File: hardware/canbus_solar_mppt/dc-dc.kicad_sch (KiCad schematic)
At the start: 22 parts

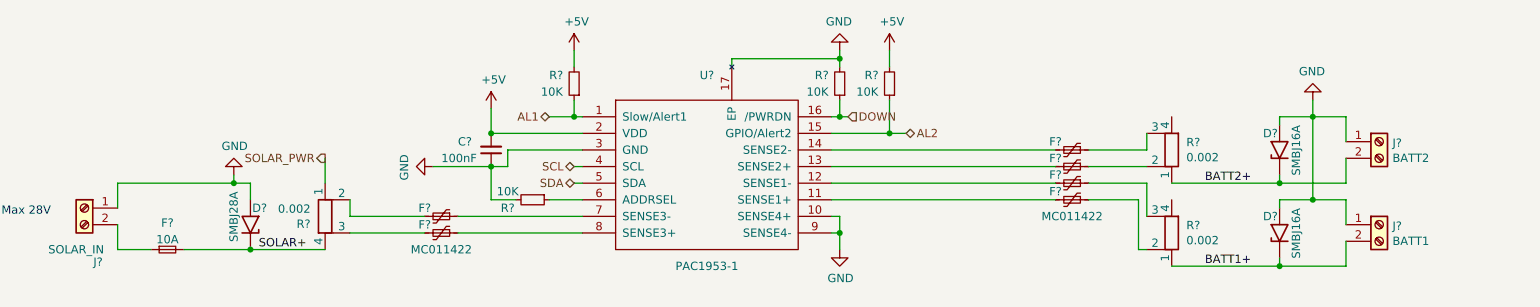
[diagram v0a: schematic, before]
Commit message: Add feedthrough capacitors as EMI filters on power inputs
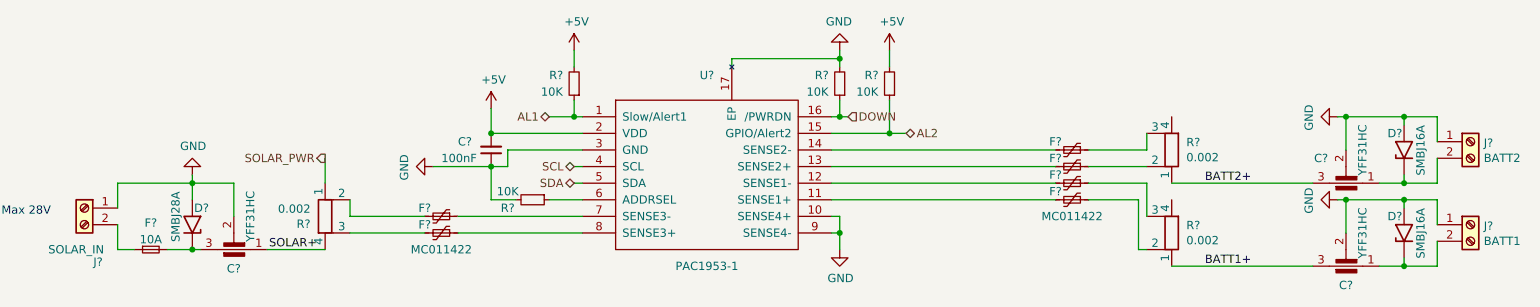
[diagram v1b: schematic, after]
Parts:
- added C? (x3): YFF31HC, local:C_filter_1206, symbol Device:C_Feedthrough
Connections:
- net BATT1+: now also C?.3; no longer D?.1 (A1), J?.2 (Pin_2)
- net BATT2+: now also C?.3; no longer D?.1 (A1), J?.2 (Pin_2)
- net GND: now also C?.2, C?.2, C?.2
- net SOLAR+: now also C?.1; no longer D?.1 (A1), F?.2
- new net: C?.1, D?.1 (A1), J?.2 (Pin_2) (x2)
- new net: C?.3, D?.1 (A1), F?.2
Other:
- moved on the sheet: D?, F?, J?

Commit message: WIP: complete DC/DC engine
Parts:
- added C?: 10µ25V, Capacitor_SMD:C_1206_3216Metric_Pad1.33x1.80mm_HandSolder, symbol Device:C_Small
- added C? (x4): 330µ35V, Capacitor_SMD:CP_Elec_10x12.6, symbol Device:C_Polarized_Small
- added C? (x2): 100nF, Capacitor_SMD:C_0805_2012Metric_Pad1.18x1.45mm_HandSolder, symbol Device:C_Small
- added C? (x2): 4.7µ50V, Capacitor_SMD:C_1206_3216Metric_Pad1.33x1.80mm_HandSolder, symbol Device:C_Small
- added C?: 100nF, Capacitor_SMD:C_1206_3216Metric_Pad1.33x1.80mm_HandSolder, symbol Device:C_Small
- added C?: 100nF50V, Capacitor_SMD:C_0805_2012Metric_Pad1.18x1.45mm_HandSolder, symbol Device:C_Small
- added C?: 22µ, Capacitor_SMD:C_1206_3216Metric_Pad1.33x1.80mm_HandSolder, symbol Device:C_Small
- added L?: 22µH, Inductor_THT:L_Toroid_Horizontal_D32.5mm_P30.00mm_Bourns_2300, symbol Device:L_Small
- added Q? (x2): SIR164ADP, Package_SO:PowerPAK_SO-8_Single, symbol q_nmos_sssgd:Q_NMOS_SSSGD
- added Q? (x2): BSS123, Package_TO_SOT_SMD:SOT-23, symbol Device:Q_NMOS_GSD
- added Q? (x4): SiSS27DN, Package_SO:Vishay_PowerPAK_1212-8_Single, symbol Transistor_FET:SiSS27DN
- added R? (x3): 56K, Resistor_THT:R_Axial_DIN0207_L6.3mm_D2.5mm_P7.62mm_Horizontal, symbol Device:R_Small
- added R? (x2): 100K, Resistor_THT:R_Axial_DIN0207_L6.3mm_D2.5mm_P7.62mm_Horizontal, symbol Device:R_Small
- added R?: 270k, Resistor_SMD:R_0805_2012Metric_Pad1.20x1.40mm_HandSolder, symbol Device:R_Small
- added R?: 56k, Resistor_SMD:R_0805_2012Metric_Pad1.20x1.40mm_HandSolder, symbol Device:R_Small
- added U?: NCP5901B, Package_SO:SOIC-8_3.9x4.9mm_P1.27mm, symbol onsemi-local:NCP5901B
- added U?: LP4951C, Package_SO:SOIC-8_3.9x4.9mm_P1.27mm, symbol texas-local:LP4951C
- F? (x6): P/N (none) -> MC011422
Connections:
- net +5V: now also R?.2
- net GND: now also C?.1, C?.1, C?.1, C?.2, C?.2, C?.2, C?.2, C?.2, C?.2, C?.2, C?.2, Q?.1 (S), Q?.2 (S), Q?.2 (S), Q?.2 (S), Q?.3 (S), R?.1, R?.2, R?.2, U?.4 (GND), U?.6 (GND)
- net SOLAR_PWR: now also C?.1, C?.1, C?.1, C?.1, C?.2, Q?.5 (D), U?.8 (In)
- net at R?.4: now also Q?.5 (D) (x2)
- new net: C?.1, C?.1, C?.1, C?.1, L?.2, Q?.5 (D), Q?.5 (D)
- new net: C?.2, U?.1 (BST)
- new net: Q?.4 (G), U?.5 (DRVL)
- new net: C?.1, L?.1, Q?.1 (S), Q?.2 (S), Q?.3 (S), Q?.5 (D), U?.7 (SW)
- new net: Q?.4 (G), U?.8 (DRVH)
- new net: Q?.3 (D), Q?.4 (G), Q?.4 (G), R?.1 (x2)
- new net: Q?.1 (S), Q?.1 (S), Q?.2 (S), Q?.2 (S), Q?.3 (S), Q?.3 (S), R?.2 (x2)
- new net: R?.1, R?.2, U?.7 (feedback)
- new net +7V: C?.2, C?.2, R?.2, U?.1 (OUT), U?.4 (VCC)
- new net BATT1_ON: Q?.1 (G), R?.1
- new net BATT2_ON: Q?.1 (G), R?.1
- new net PWM: U?.2 (PWM)
- new net PWM_OFF: U?.3 (shutdown)
- new net PWM_OK: R?.1, U?.3 (EN), U?.5 (/Error)
- no-connect marks 0 -> 2
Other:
- note added: "(270/56 + 1) * 1.235 = 7.18V"
- moved on the sheet: R?

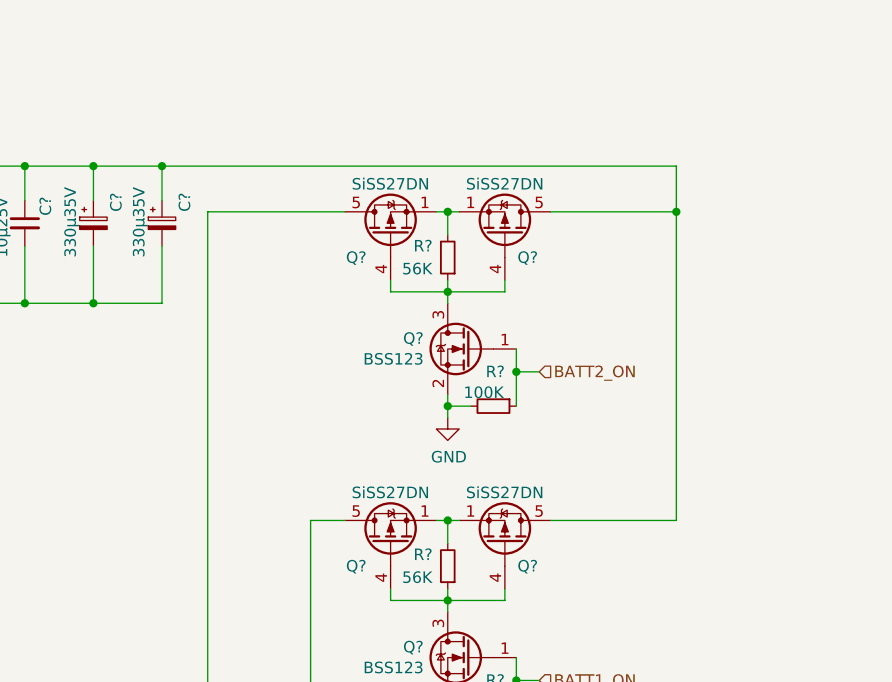
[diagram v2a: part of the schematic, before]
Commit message: Add a voltage reference for the pic18 comparator, and a matching voltage divider at DC/DC output.
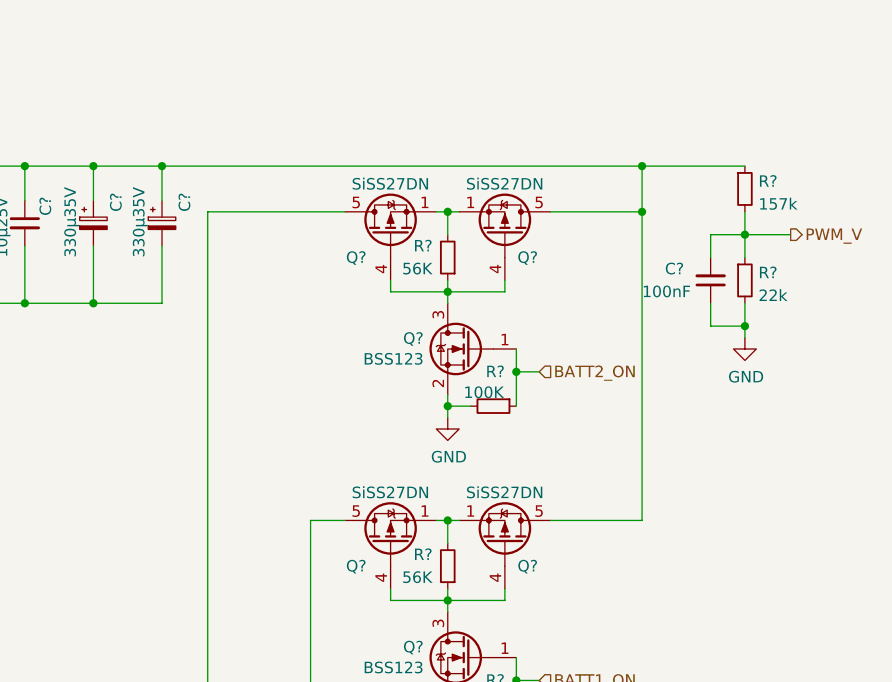
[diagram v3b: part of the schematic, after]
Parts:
- added C?: 100nF, Capacitor_SMD:C_0805_2012Metric_Pad1.18x1.45mm_HandSolder, symbol Device:C_Small
- added R?: 22k, Resistor_SMD:R_0805_2012Metric_Pad1.20x1.40mm_HandSolder, symbol Device:R_Small
- added R?: 157k, Resistor_SMD:R_0805_2012Metric_Pad1.20x1.40mm_HandSolder, symbol Device:R_Small
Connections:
- net GND: now also C?.1, R?.2
- net at C?.1, C?.1, C?.1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: now also R?.1
- new net PWM_V: C?.2, R?.1, R?.2
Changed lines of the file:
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@@
   (junction (at 196.85 58.42) (diameter 0) (color 0 0 0 0)
   )
+  (junction (at 269.24 66.04) (diameter 0) (color 0 0 0 0)
+  )
   (junction (at 236.22 142.24) (diameter 0) (color 0 0 0 0)
   )
@@
   (junction (at 52.07 62.23) (diameter 0) (color 0 0 0 0)
   )
-  (junction (at 261.62 63.5) (diameter 0) (color 0 0 0 0)
+  (junction (at 257.81 63.5) (diameter 0) (color 0 0 0 0)
   )
   (junction (at 236.22 119.38) (diameter 0) (color 0 0 0 0)
@@
   (junction (at 157.48 58.42) (diameter 0) (color 0 0 0 0)
   )
+  (junction (at 269.24 76.2) (diameter 0) (color 0 0 0 0)
+  )
   (junction (at 62.23 29.21) (diameter 0) (color 0 0 0 0)
   )
@@
   )
   (junction (at 245.11 129.54) (diameter 0) (color 0 0 0 0)
+  )
+  (junction (at 257.81 58.42) (diameter 0) (color 0 0 0 0)
   )
   (junction (at 114.3 73.66) (diameter 0) (color 0 0 0 0)
@@
   (no_connect (at 66.04 59.69))
   (no_connect (at 93.98 57.15))
+  (wire (pts (xy 269.24 63.5) (xy 269.24 66.04))
+    (stroke (width 0) (type default) (color 0 0 0 0))
+  )
   (wire (pts (xy 157.48 147.32) (xy 158.75 147.32))
     (stroke (width 0) (type default) (color 0 0 0 0))
@@
     (stroke (width 0) (type default) (color 0 0 0 0))
   )
+  (wire (pts (xy 269.24 66.04) (xy 274.32 66.04))
+    (stroke (width 0) (type default) (color 0 0 0 0))
+  )
+  (wire (pts (xy 269.24 76.2) (xy 269.24 77.47))
+    (stroke (width 0) (type default) (color 0 0 0 0))
+  )
   (wire (pts (xy 162.56 58.42) (xy 162.56 57.15))
     (stroke (width 0) (type default) (color 0 0 0 0))
@@
     (stroke (width 0) (type default) (color 0 0 0 0))
   )
+  (wire (pts (xy 269.24 66.04) (xy 265.43 66.04))
+    (stroke (width 0) (type default) (color 0 0 0 0))
+  )
   (wire (pts (xy 242.57 106.68) (xy 242.57 105.41))
     (stroke (width 0) (type default) (color 0 0 0 0))
@@
     (stroke (width 0) (type default) (color 0 0 0 0))
   )
-  (wire (pts (xy 261.62 63.5) (xy 247.65 63.5))
+  (wire (pts (xy 257.81 63.5) (xy 247.65 63.5))
     (stroke (width 0) (type default) (color 0 0 0 0))
   )
@@
     (stroke (width 0) (type default) (color 0 0 0 0))
   )
+  (wire (pts (xy 269.24 66.04) (xy 269.24 68.58))
+    (stroke (width 0) (type default) (color 0 0 0 0))
+  )
   (wire (pts (xy 250.19 129.54) (xy 250.19 133.35))
     (stroke (width 0) (type default) (color 0 0 0 0))
@@
     (stroke (width 0) (type default) (color 0 0 0 0))
   )
-  (wire (pts (xy 261.62 58.42) (xy 261.62 63.5))
+  (wire (pts (xy 265.43 66.04) (xy 265.43 68.58))
+    (stroke (width 0) (type default) (color 0 0 0 0))
+  )
+  (wire (pts (xy 257.81 58.42) (xy 257.81 63.5))
     (stroke (width 0) (type default) (color 0 0 0 0))
   )
@@
     (stroke (width 0) (type default) (color 0 0 0 0))
   )
-  (wire (pts (xy 204.47 58.42) (xy 261.62 58.42))
+  (wire (pts (xy 204.47 58.42) (xy 257.81 58.42))
     (stroke (width 0) (type default) (color 0 0 0 0))
   )
@@
     (stroke (width 0) (type default) (color 0 0 0 0))
   )
-  (wire (pts (xy 261.62 97.79) (xy 261.62 63.5))
+  (wire (pts (xy 257.81 97.79) (xy 257.81 63.5))
     (stroke (width 0) (type default) (color 0 0 0 0))
   )
@@
     (stroke (width 0) (type default) (color 0 0 0 0))
   )
+  (wire (pts (xy 269.24 73.66) (xy 269.24 76.2))
+    (stroke (width 0) (type default) (color 0 0 0 0))
+  )
+  (wire (pts (xy 265.43 76.2) (xy 269.24 76.2))
+    (stroke (width 0) (type default) (color 0 0 0 0))
+  )
   (wire (pts (xy 189.23 73.66) (xy 181.61 73.66))
     (stroke (width 0) (type default) (color 0 0 0 0))
@@
     (stroke (width 0) (type default) (color 0 0 0 0))
   )
+  (wire (pts (xy 265.43 73.66) (xy 265.43 76.2))
+    (stroke (width 0) (type default) (color 0 0 0 0))
+  )
   (wire (pts (xy 245.11 139.7) (xy 250.19 139.7))
     (stroke (width 0) (type default) (color 0 0 0 0))
@@
     (stroke (width 0) (type default) (color 0 0 0 0))
   )
+  (wire (pts (xy 257.81 58.42) (xy 269.24 58.42))
+    (stroke (width 0) (type default) (color 0 0 0 0))
+  )
   (wire (pts (xy 245.11 138.43) (xy 245.11 139.7))
     (stroke (width 0) (type default) (color 0 0 0 0))
@@
     (stroke (width 0) (type default) (color 0 0 0 0))
   )
-  (wire (pts (xy 247.65 97.79) (xy 261.62 97.79))
+  (wire (pts (xy 247.65 97.79) (xy 257.81 97.79))
     (stroke (width 0) (type default) (color 0 0 0 0))
   )
@@
   (label "BATT1+" (at 223.52 152.4 0)
     (effects (font (size 1.27 1.27)) (justify left bottom))
+  )
+  (hierarchical_label "PWM_V" (shape output) (at 274.32 66.04 0)
+    (effects (font (size 1.27 1.27)) (justify left))
   )
   (hierarchical_label "PWM" (shape input) (at 116.84 58.42 180)
@@
     (pin "1")
   )
+  (symbol (lib_id "power:GND") (at 269.24 77.47 0) (unit 1)
+    (in_bom yes) (on_board yes)
+    (property "Reference" "#PWR?" (id 0) (at 269.24 83.82 0)
+      (effects (font (size 1.27 1.27)) hide)
+    )
+    (property "Value" "GND" (id 1) (at 269.367 81.8642 0))
+    (property "Footprint" "" (id 2) (at 269.24 77.47 0)
+      (effects (font (size 1.27 1.27)) hide)
+    )
+    (property "Datasheet" "" (id 3) (at 269.24 77.47 0)
+      (effects (font (size 1.27 1.27)) hide)
+    )
+    (pin "1")
+  )
   (symbol (lib_id "Device:R_Small") (at 241.3 85.09 270) (unit 1)
     (in_bom yes) (on_board yes)
@@
     )
     (property "P/N" "GRM31CR71H475KA12L" (id 4) (at 88.9 35.56 0)
+      (effects (font (size 1.27 1.27)) hide)
+    )
+    (pin "1")
+    (pin "2")
+  )
+  (symbol (lib_id "Device:R_Small") (at 269.24 71.12 0) (unit 1)
+    (in_bom yes) (on_board yes) (fields_autoplaced)
+    (property "Reference" "R?" (id 0) (at 270.7386 70.2853 0)
+      (effects (font (size 1.27 1.27)) (justify left))
+    )
+    (property "Value" "22k" (id 1) (at 270.7386 72.8222 0)
+      (effects (font (size 1.27 1.27)) (justify left))
+    )
+    (property "Footprint" "Resistor_SMD:R_0805_2012Metric_Pad1.20x1.40mm_HandSolder" (id 2) (at 269.24 71.12 0)
+      (effects (font (size 1.27 1.27)) hide)
+    )
+    (property "Datasheet" "~" (id 3) (at 269.24 71.12 0)
+      (effects (font (size 1.27 1.27)) hide)
+    )
+    (pin "1")
+    (pin "2")
+  )
+  (symbol (lib_id "Device:R_Small") (at 269.24 60.96 0) (unit 1)
+    (in_bom yes) (on_board yes) (fields_autoplaced)
+    (property "Reference" "R?" (id 0) (at 270.7386 60.1253 0)
+      (effects (font (size 1.27 1.27)) (justify left))
+    )
+    (property "Value" "157k" (id 1) (at 270.7386 62.6622 0)
+      (effects (font (size 1.27 1.27)) (justify left))
+    )
+    (property "Footprint" "Resistor_SMD:R_0805_2012Metric_Pad1.20x1.40mm_HandSolder" (id 2) (at 269.24 60.96 0)
+      (effects (font (size 1.27 1.27)) hide)
+    )
+    (property "Datasheet" "~" (id 3) (at 269.24 60.96 0)
       (effects (font (size 1.27 1.27)) hide)
     )
@@
     (pin "9")
   )
+  (symbol (lib_id "Device:C_Small") (at 265.43 71.12 180) (unit 1)
+    (in_bom yes) (on_board yes)
+    (property "Reference" "C?" (id 0) (at 260.35 69.85 0)
+      (effects (font (size 1.27 1.27)) (justify right))
+    )
+    (property "Value" "100nF" (id 1) (at 257.81 72.39 0)
+      (effects (font (size 1.27 1.27)) (justify right))
+    )
+    (property "Footprint" "Capacitor_SMD:C_0805_2012Metric_Pad1.18x1.45mm_HandSolder" (id 2) (at 265.43 71.12 0)
+      (effects (font (size 1.27 1.27)) hide)
+    )
+    (property "Datasheet" "~" (id 3) (at 265.43 71.12 0)
+      (effects (font (size 1.27 1.27)) hide)
+    )
+    (pin "1")
+    (pin "2")
+  )
   (symbol (lib_id "Device:C_Feedthrough") (at 66.04 147.32 180) (unit 1)
